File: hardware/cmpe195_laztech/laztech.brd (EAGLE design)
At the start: 68.2 x 61 mm, 7 parts

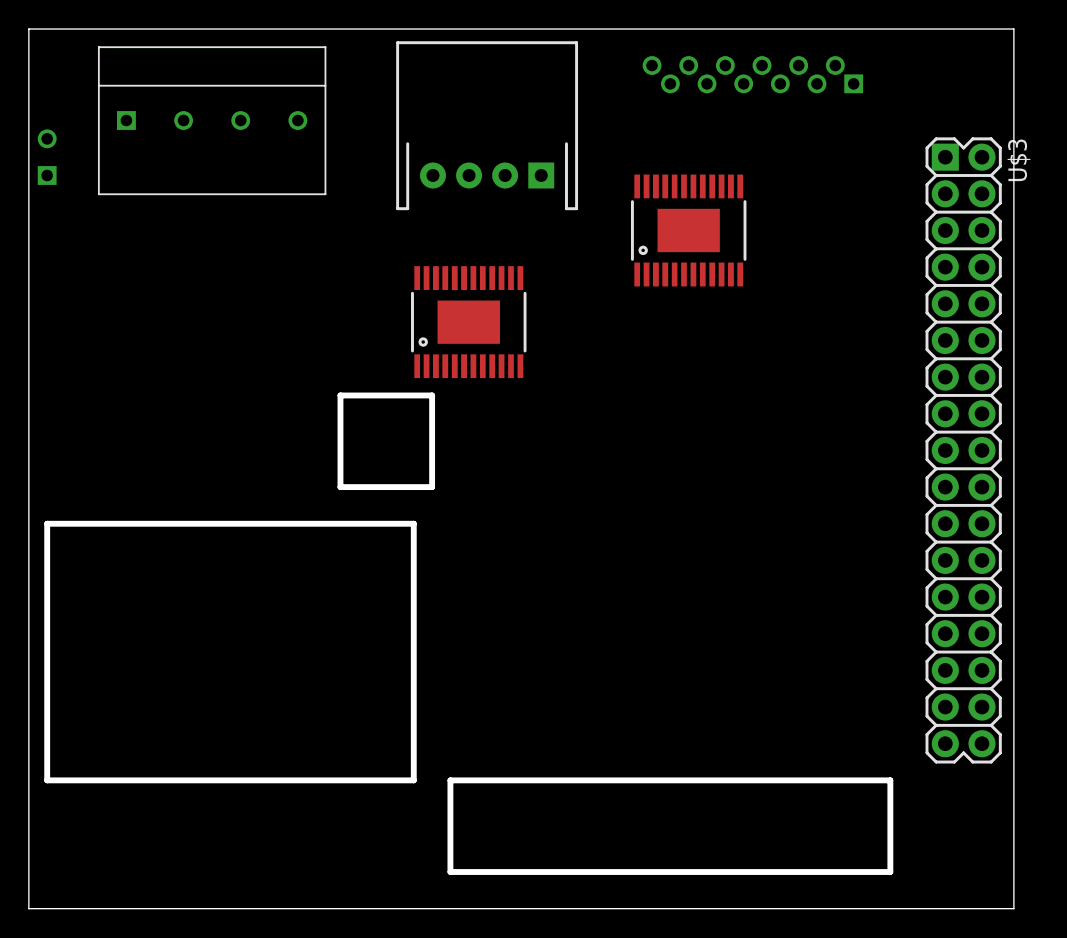
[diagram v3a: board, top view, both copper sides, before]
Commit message: Fixed more parts in library.
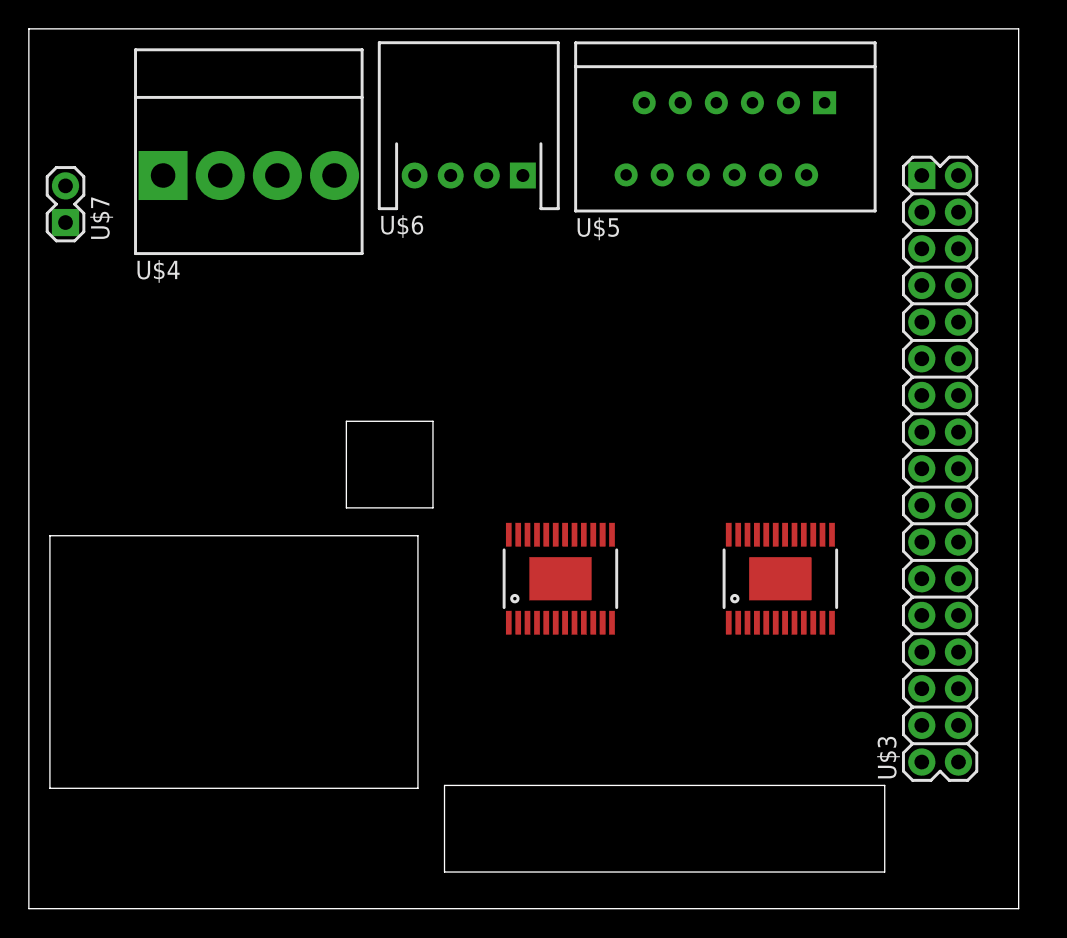
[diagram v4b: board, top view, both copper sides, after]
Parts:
- U$4: value K40KK -> K40-PWR; device laztech_parts:KK396-4 -> laztech_parts:MOLEX-KK396-4-RA
- U$5: value K40FFC -> K40-X; device laztech_parts:FFC-12 -> laztech_parts:MOLEX-FFC-12-RA
- U$6: value K40JST -> K40-Y; device laztech_parts:JST-XH-4-RA -> laztech_parts:JST-XH-4_RA
- U$7: device laztech_parts:M1X2 -> laztech_parts:1X02
- moved U$1 25.0 mm to (52.1, 22.9)
- moved U$2 18.9 mm to (36.8, 22.9)
- moved U$5 9.67 mm to (48.3, 53.3), turned to 0 degrees
- moved U$4 4.58 mm to (15.2, 50.8)
- moved U$7 2.36 mm to (2.54, 48.8)
- moved U$3 2.07 mm to (63.1, 30.5)
- moved U$6 1.27 mm to (30.5, 50.8)
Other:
- board size 68.2 x 61 mm -> 68.6 x 61 mm

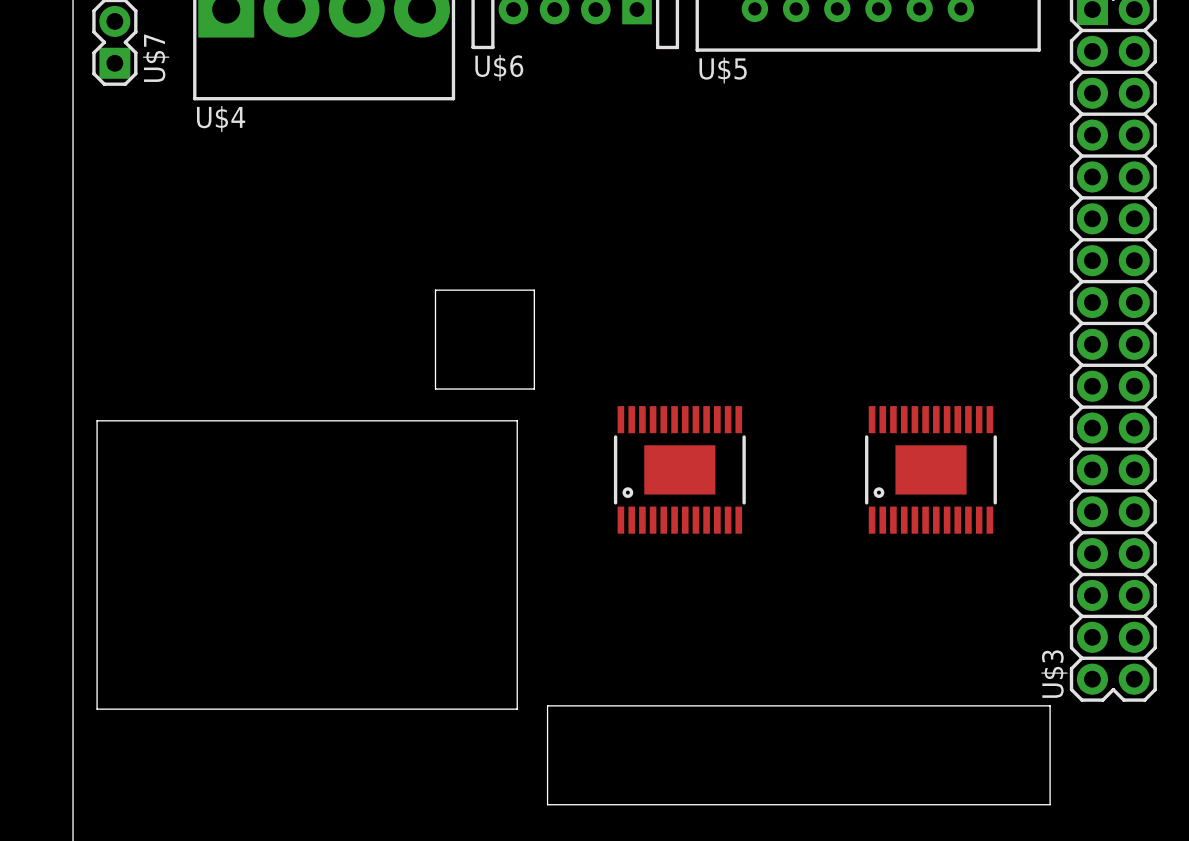
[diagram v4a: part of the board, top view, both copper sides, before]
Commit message: Added capacitors to sch and brd.
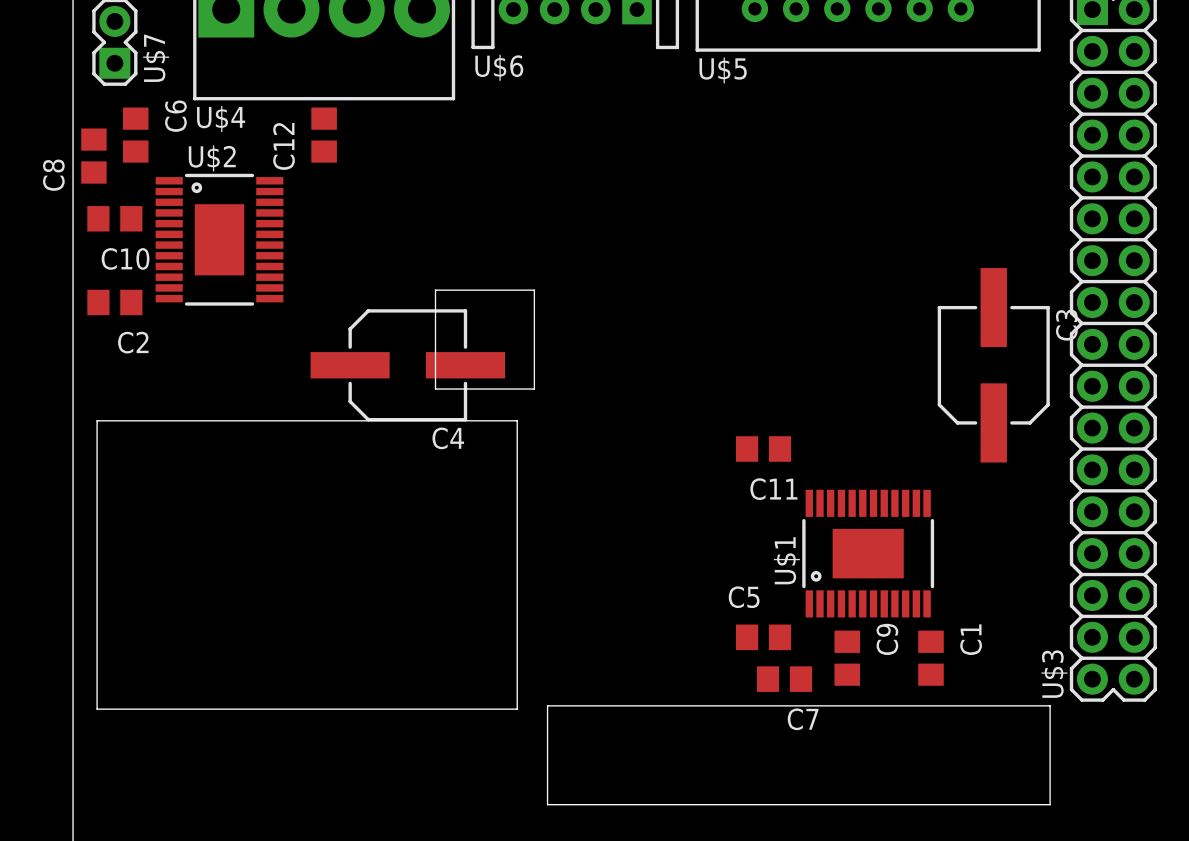
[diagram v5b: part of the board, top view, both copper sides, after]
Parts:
- added C1, C10, C11, C12, C2, C5, C6, C7, C8, C9: (no value), laztech_parts:C2012
- added C3, C4: (no value), laztech_parts:C6358R
- U$1, U$2: device laztech_parts:TSSOP-24 -> laztech_parts:ETSSOP-24
- moved U$2 31.2 mm to (8.89, 36.8), turned to 270 degrees
- moved U$1 6.35 mm to (48.3, 17.8)
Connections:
- new net N$26: C10.1, U$2.4
- new net N$27: C6.1, U$2.1
- new net N$28: C6.2, U$2.2
- new net N$29: C8.1, U$2.3
- new net N$30: C9.1, U$1.4
- new net N$31: C5.1, U$1.1
- new net N$32: C5.2, U$1.2
- new net N$33: C7.1, U$1.3
- net +3V3: now also C1.1, C2.1
- net GND: now also C1.2, C10.2, C11.2, C12.2, C2.2, C3.2, C4.2, C9.2
- net N$9: now also C11.1, C12.1, C3.1, C4.1, C7.2, C8.2

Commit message: Added LM317.
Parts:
- added C13: (no value), laztech_parts:C2012
- added U$8: LM317, laztech_parts:SOIC-8
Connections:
- removed net N$9: C11.1, C12.1, C3.1, C4.1, C7.2, C8.2, U$1.16, U$1.21, U$2.16, U$2.21, U$4.4
- new net +24V: C11.1, C12.1, C13.1, C3.1, C4.1, C7.2, C8.2, U$1.16, U$1.21, U$2.16, U$2.21, U$4.4, U$8.1
- net GND: now also C13.2
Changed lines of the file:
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@@
 <element name="C11" library="laztech_parts" package="C2012" value="" x="41.91" y="24.13" rot="R180"/>
 <element name="C12" library="laztech_parts" package="C2012" value="" x="15.24" y="43.18" rot="R90"/>
+<element name="U$8" library="laztech_parts" package="SOIC-8" value="LM317" x="24.13" y="5.08"/>
+<element name="C13" library="laztech_parts" package="C2012" value="" x="20.32" y="1.27" rot="R180"/>
 </elements>
 <signals>
@@
 <contactref element="C11" pad="2"/>
 <contactref element="C3" pad="2"/>
+<contactref element="C13" pad="2"/>
 <wire x1="48.885" y1="50.84" x2="64.41" y2="48.26" width="0" layer="19" extent="1-1"/>
-<wire x1="55.88" y1="25.71" x2="48.885" y2="50.84" width="0" layer="19" extent="1-1"/>
+<wire x1="55.88" y1="25.71" x2="64.41" y2="48.26" width="0" layer="19" extent="1-1"/>
 <wire x1="51.835" y1="20.83" x2="55.88" y2="25.71" width="0" layer="19" extent="1-1"/>
 <wire x1="48.26" y1="17.78" x2="51.835" y2="20.83" width="0" layer="19" extent="1-1"/>
@@
 <wire x1="15.24" y1="44.18" x2="11.94" y2="40.405" width="0" layer="19" extent="1-1"/>
 <wire x1="1.54" y1="33.02" x2="1.54" y2="38.1" width="0" layer="19" extent="1-1"/>
-<wire x1="17.22" y1="50.8" x2="16.82" y2="29.21" width="0" layer="19" extent="1-1"/>
-<wire x1="2.54" y1="50.08" x2="17.22" y2="50.8" width="0" layer="19" extent="1-1"/>
+<wire x1="17.22" y1="50.8" x2="15.24" y2="44.18" width="0" layer="19" extent="1-1"/>
+<wire x1="2.54" y1="50.08" x2="1.54" y2="38.1" width="0" layer="19" extent="1-1"/>
+<wire x1="19.32" y1="1.27" x2="16.82" y2="29.21" width="0" layer="19" extent="1-1"/>
 </signal>
 <signal name="+3V3">
@@
 <wire x1="1.27" y1="40.91" x2="5.84" y2="39.105" width="0" layer="19" extent="1-1"/>
 </signal>
-<signal name="N$9">
-<contactref element="U$4" pad="4"/>
+<signal name="N$30">
+<contactref element="U$1" pad="4"/>
+<contactref element="C9" pad="1"/>
+<wire x1="46.99" y1="12.43" x2="46.635" y2="14.73" width="0" layer="19" extent="1-1"/>
+</signal>
+<signal name="N$31">
+<contactref element="U$1" pad="1"/>
+<contactref element="C5" pad="1"/>
+<wire x1="40.91" y1="12.7" x2="44.685" y2="14.73" width="0" layer="19" extent="1-1"/>
+</signal>
+<signal name="N$32">
+<contactref element="C5" pad="2"/>
+<contactref element="U$1" pad="2"/>
+<wire x1="42.91" y1="12.7" x2="45.335" y2="14.73" width="0" layer="19" extent="1-1"/>
+</signal>
+<signal name="N$33">
+<contactref element="U$1" pad="3"/>
+<contactref element="C7" pad="1"/>
+<wire x1="44.18" y1="10.16" x2="45.985" y2="14.73" width="0" layer="19" extent="1-1"/>
+</signal>
+<signal name="+24V">
+<contactref element="U$8" pad="1"/>
 <contactref element="C12" pad="1"/>
 <contactref element="C4" pad="1"/>
-<contactref element="U$1" pad="16"/>
-<contactref element="U$1" pad="21"/>
 <contactref element="U$2" pad="16"/>
 <contactref element="U$2" pad="21"/>
 <contactref element="C8" pad="2"/>
+<contactref element="U$4" pad="4"/>
+<contactref element="U$1" pad="16"/>
+<contactref element="U$1" pad="21"/>
 <contactref element="C7" pad="2"/>
 <contactref element="C11" pad="1"/>
 <contactref element="C3" pad="1"/>
+<contactref element="C13" pad="1"/>
 <wire x1="49.885" y1="20.83" x2="55.88" y2="32.71" width="0" layer="19" extent="1-1"/>
 <wire x1="46.635" y1="20.83" x2="49.885" y2="20.83" width="0" layer="19" extent="1-1"/>
@@
 <wire x1="11.94" y1="38.455" x2="11.94" y2="35.205" width="0" layer="19" extent="1-1"/>
 <wire x1="15.24" y1="42.18" x2="11.94" y2="38.455" width="0" layer="19" extent="1-1"/>
+<wire x1="21.18" y1="50.8" x2="15.24" y2="42.18" width="0" layer="19" extent="1-1"/>
 <wire x1="1.27" y1="42.91" x2="11.94" y2="38.455" width="0" layer="19" extent="1-1"/>
-<wire x1="21.18" y1="50.8" x2="23.82" y2="29.21" width="0" layer="19" extent="1-1"/>
-</signal>
-<signal name="N$30">
-<contactref element="U$1" pad="4"/>
-<contactref element="C9" pad="1"/>
-<wire x1="46.99" y1="12.43" x2="46.635" y2="14.73" width="0" layer="19" extent="1-1"/>
-</signal>
-<signal name="N$31">
-<contactref element="U$1" pad="1"/>
-<contactref element="C5" pad="1"/>
-<wire x1="40.91" y1="12.7" x2="44.685" y2="14.73" width="0" layer="19" extent="1-1"/>
-</signal>
-<signal name="N$32">
-<contactref element="C5" pad="2"/>
-<contactref element="U$1" pad="2"/>
-<wire x1="42.91" y1="12.7" x2="45.335" y2="14.73" width="0" layer="19" extent="1-1"/>
-</signal>
-<signal name="N$33">
-<contactref element="U$1" pad="3"/>
-<contactref element="C7" pad="1"/>
-<wire x1="44.18" y1="10.16" x2="45.985" y2="14.73" width="0" layer="19" extent="1-1"/>
+<wire x1="22.505" y1="2.03" x2="23.82" y2="29.21" width="0" layer="19" extent="1-1"/>
+<wire x1="21.32" y1="1.27" x2="22.505" y2="2.03" width="0" layer="19" extent="1-1"/>
 </signal>
 </signals>
